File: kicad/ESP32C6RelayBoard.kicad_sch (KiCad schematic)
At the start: 118 parts, among them IC1 SPX1117M3-L-3-3_TR, J1 Screw_Terminal_01x02, J10 Screw_Terminal_01x03, J11 Screw_Terminal_01x03, J12 Screw_Terminal_01x03, J13 Screw_Terminal_01x03, J2 Conn_02x08_Odd_Even, J3 Screw_Terminal_01x02, J4 Screw_Terminal_01x02, J5 10118192-0001LF, J6 Screw_Terminal_01x02, J7 Screw_Terminal_01x02, J8 Screw_Terminal_01x03, J9 Screw_Terminal_01x03, K1 G5RL-K1-E-DC12, K2 G5RL-K1-E-DC12, K3 G5RL-K1-E-DC12, K4 G5RL-K1-E-DC12, Q1 FDN302P, U1 AP62300Z6-7, U10 INA232AIDDFR, U11 74HC237, U12 INA232AIDDFR, U13 FAN3241TMX, U14 FAN3241TMX, U2 ESP32-C6-MINI-1/U, U3 434133025816, U4 434133025816, U5 ESD401DPYR, U6 ESD401DPYR, U7 ESD401DPYR, U8 FAN3241TMX, U9 FAN3241TMX

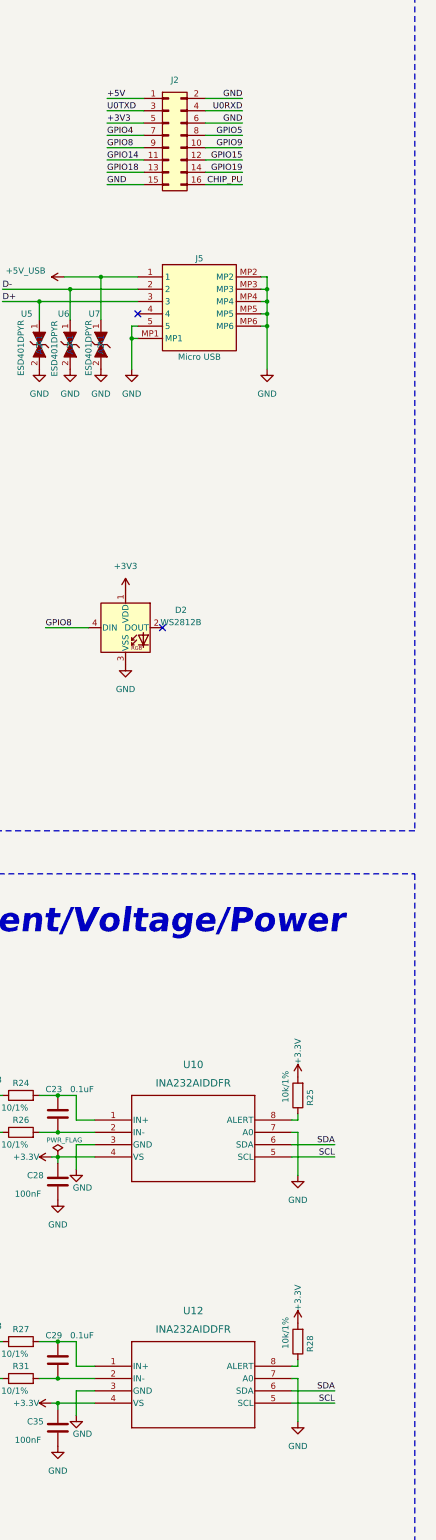
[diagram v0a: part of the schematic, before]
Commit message: Exposed also SCL and SDO on EXT connector
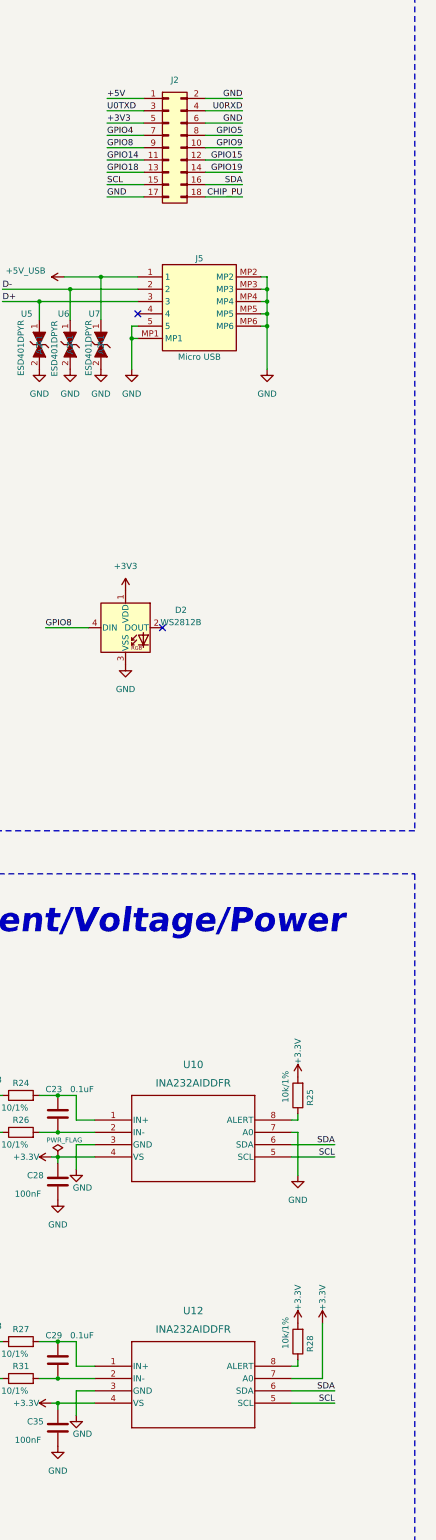
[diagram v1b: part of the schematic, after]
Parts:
- removed J2: Conn_02x08_Odd_Even, Connector_PinHeader_2.54mm:PinHeader_2x08_P2.54mm_Vertical, symbol Connector_Generic:Conn_02x08_Odd_Even
- added J2: Conn_02x09_Odd_Even, Connector_PinHeader_2.54mm:PinHeader_2x09_P2.54mm_Vertical, symbol Connector_Generic:Conn_02x09_Odd_Even
- U8: footprint (none) -> Onsemi:SOIC127P600X175-8N
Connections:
- net +3.3V: now also U12.7 (A0)
- net +3V3: now also J2.5 (Pin_5)
- net +5V: now also J2.1 (Pin_1)
- net CHIP_PU: now also J2.18 (Pin_18)
- net GND: now also J2.17 (Pin_17), J2.2 (Pin_2), J2.6 (Pin_6); no longer U12.7 (A0)
- net GPIO14: now also J2.11 (Pin_11)
- net GPIO15: now also J2.12 (Pin_12)
- net GPIO18: now also J2.13 (Pin_13)
- net GPIO19: now also J2.14 (Pin_14)
- net GPIO4: now also J2.7 (Pin_7)
- net GPIO5: now also J2.8 (Pin_8)
- net GPIO8: now also J2.9 (Pin_9)
- net GPIO9: now also J2.10 (Pin_10)
- net SCL: now also J2.15 (Pin_15)
- net SDA: now also J2.16 (Pin_16)
- net U0RXD: now also J2.4 (Pin_4)
- net U0TXD: now also J2.3 (Pin_3)
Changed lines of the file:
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@@
     (stroke (width 0) (type default))
   )
+  (wire (pts (xy 421.64 86.36) (xy 429.26 86.36))
+    (stroke (width 0) (type default))
+  )
   (wire (pts (xy 394.97 327.66) (xy 398.78 327.66))
     (stroke (width 0) (type default))
@@
     (stroke (width 0) (type default))
   )
-  (wire (pts (xy 421.64 83.82) (xy 429.26 83.82))
-    (stroke (width 0) (type default))
-  )
   (wire (pts (xy 128.27 152.4) (xy 128.27 154.94))
     (stroke (width 0) (type default))
@@
     (stroke (width 0) (type default))
   )
+  (wire (pts (xy 421.64 83.82) (xy 429.26 83.82))
+    (stroke (width 0) (type default))
+  )
   (wire (pts (xy 400.05 102.87) (xy 400.05 111.76))
     (stroke (width 0) (type default))
@@
     (stroke (width 0) (type default))
   )
-  (wire (pts (xy 439.42 330.2) (xy 440.69 330.2))
+  (wire (pts (xy 439.42 330.2) (xy 445.77 330.2))
     (stroke (width 0) (type default))
   )
@@
     (stroke (width 0) (type default))
   )
+  (wire (pts (xy 401.32 86.36) (xy 408.94 86.36))
+    (stroke (width 0) (type default))
+  )
   (wire (pts (xy 104.14 109.22) (xy 124.46 109.22))
     (stroke (width 0) (type default))
@@
     (stroke (width 0) (type default))
   )
-  (wire (pts (xy 440.69 330.2) (xy 440.69 339.09))
+  (wire (pts (xy 445.77 330.2) (xy 445.77 318.77))
     (stroke (width 0) (type default))
   )
@@
     (stroke (width 0) (type default))
   )
-  (wire (pts (xy 401.32 83.82) (xy 408.94 83.82))
-    (stroke (width 0) (type default))
-  )
   (wire (pts (xy 341.63 173.99) (xy 345.44 173.99))
     (stroke (width 0) (type default))
@@
     (stroke (width 0) (type default))
   )
+  (wire (pts (xy 401.32 83.82) (xy 408.94 83.82))
+    (stroke (width 0) (type default))
+  )
   (wire (pts (xy 110.49 85.09) (xy 129.54 85.09))
     (stroke (width 0) (type default))
@@
     (effects (font (size 1.27 1.27)) (justify right bottom))
   )
+  (label "GND" (at 401.32 86.36 0) (fields_autoplaced)
+    (effects (font (size 1.27 1.27)) (justify left bottom))
+  )
   (label "S{slash}R" (at 363.22 107.95 180) (fields_autoplaced)
     (effects (font (size 1.27 1.27)) (justify right bottom))
   )
+  (label "SDA" (at 429.26 83.82 180) (fields_autoplaced)
+    (effects (font (size 1.27 1.27)) (justify right bottom))
+  )
   (label "R0R" (at 77.47 306.07 180) (fields_autoplaced)
     (effects (font (size 1.27 1.27)) (justify right bottom))
@@
     (effects (font (size 1.27 1.27)) (justify left bottom))
   )
-  (label "GND" (at 401.32 83.82 0) (fields_autoplaced)
-    (effects (font (size 1.27 1.27)) (justify left bottom))
-  )
   (label "R3R" (at 219.71 344.17 0) (fields_autoplaced)
     (effects (font (size 1.27 1.27)) (justify left bottom))
@@
     (effects (font (size 1.27 1.27)) (justify left bottom))
   )
-  (label "CHIP_PU" (at 429.26 83.82 180) (fields_autoplaced)
-    (effects (font (size 1.27 1.27)) (justify right bottom))
-  )
   (label "GND" (at 429.26 71.12 180) (fields_autoplaced)
     (effects (font (size 1.27 1.27)) (justify right bottom))
@@
     (effects (font (size 1.27 1.27)) (justify right bottom))
   )
+  (label "SCL" (at 401.32 83.82 0) (fields_autoplaced)
+    (effects (font (size 1.27 1.27)) (justify left bottom))
+  )
   (label "D-" (at 379.73 105.41 0) (fields_autoplaced)
     (effects (font (size 1.27 1.27)) (justify left bottom))
@@
     (effects (font (size 1.27 1.27)) (justify right bottom))
   )
+  (label "CHIP_PU" (at 429.26 86.36 180) (fields_autoplaced)
+    (effects (font (size 1.27 1.27)) (justify right bottom))
+  )
   (label "ADC0" (at 283.21 72.39 0) (fields_autoplaced)
     (effects (font (size 1.27 1.27)) (justify left bottom))
@@
     )
   )
+  (symbol (lib_id "power:+3.3V") (at 445.77 318.77 0) (unit 1)
+    (in_bom yes) (on_board yes) (dnp no)
+    (property "Reference" "#PWR087" (at 445.77 322.58 0)
+      (effects (font (size 1.27 1.27)) hide)
+    )
+    (property "Value" "+3.3V" (at 445.77 316.23 90)
+      (effects (font (size 1.27 1.27)) (justify left))
+    )
+    (property "Footprint" "" (at 445.77 318.77 0)
+      (effects (font (size 1.27 1.27)) hide)
+    )
+    (property "Datasheet" "" (at 445.77 318.77 0)
+      (effects (font (size 1.27 1.27)) hide)
+    )
+    (pin "1")
+    (instances
+      (project "ESP32C6RelayBoard"
+        (path "/c75bdf3d-fde8-4fe0-9d0f-06bd3290cb63"
+          (reference "#PWR087") (unit 1)
+        )
+      )
+    )
+  )
   (symbol (lib_id "power:GND") (at 269.24 285.75 0) (unit 1)
     (in_bom yes) (on_board yes) (dnp no) (fields_autoplaced)
@@
     )
   )
+  (symbol (lib_id "Connector_Generic:Conn_02x09_Odd_Even") (at 414.02 76.2 0) (unit 1)
+    (in_bom yes) (on_board yes) (dnp no) (fields_autoplaced)
+    (property "Reference" "J2" (at 415.29 62.23 0)
+      (effects (font (size 1.27 1.27)))
+    )
+    (property "Value" "Conn_02x09_Odd_Even" (at 415.29 64.77 0)
+      (effects (font (size 1.27 1.27)) hide)
+    )
+    (property "Footprint" "Connector_PinHeader_2.54mm:PinHeader_2x09_P2.54mm_Vertical" (at 414.02 76.2 0)
+      (effects (font (size 1.27 1.27)) hide)
+    )
+    (property "Datasheet" "~" (at 414.02 76.2 0)
+      (effects (font (size 1.27 1.27)) hide)
+    )
+    (property "Number" "10129381-918001BLF" (at 414.02 76.2 0)
+      (effects (font (size 1.27 1.27)) hide)
+    )
+    (pin "16")
+    (pin "2")
+    (pin "3")
+    (pin "10")
+    (pin "15")
+    (pin "5")
+    (pin "7")
+    (pin "6")
+    (pin "11")
+    (pin "13")
+    (pin "9")
+    (pin "4")
+    (pin "1")
+    (pin "8")
+    (pin "14")
+    (pin "12")
+    (pin "18")
+    (pin "17")
+    (instances
+      (project "ESP32C6RelayBoard"
+        (path "/c75bdf3d-fde8-4fe0-9d0f-06bd3290cb63"
+          (reference "J2") (unit 1)
+        )
+      )
+    )
+  )
   (symbol (lib_id "Omron-G5RL:G5RL-K1-E-DC5_1") (at 311.15 294.64 270) (mirror x) (unit 1)
     (in_bom yes) (on_board yes) (dnp no)
@@
       (effects (font (size 1.27 1.27)))
     )
-    (property "Footprint" "" (at 123.19 273.05 0)
+    (property "Footprint" "Onsemi:SOIC127P600X175-8N" (at 123.19 273.05 0)
       (effects (font (size 1.27 1.27)) (justify bottom) hide)
     )
@@
     )
   )
-  (symbol (lib_id "power:GND") (at 440.69 339.09 0) (unit 1)
-    (in_bom yes) (on_board yes) (dnp no) (fields_autoplaced)
-    (property "Reference" "#PWR074" (at 440.69 345.44 0)
-      (effects (font (size 1.27 1.27)) hide)
-    )
-    (property "Value" "GND" (at 440.69 344.17 0)
-      (effects (font (size 1.27 1.27)))
-    )
-    (property "Footprint" "" (at 440.69 339.09 0)
-      (effects (font (size 1.27 1.27)) hide)
-    )
-    (property "Datasheet" "" (at 440.69 339.09 0)
-      (effects (font (size 1.27 1.27)) hide)
-    )
-    (pin "1")
-    (instances
-      (project "ESP32C6RelayBoard"
-        (path "/c75bdf3d-fde8-4fe0-9d0f-06bd3290cb63"
-          (reference "#PWR074") (unit 1)
-        )
-      )
-    )
-  )
   (symbol (lib_id "power:PWR_FLAG") (at 125.73 321.31 0) (unit 1)
     (in_bom yes) (on_board yes) (dnp no)
@@
         )
       )
-    )
-  )
-  (symbol (lib_id "Connector_Generic:Conn_02x08_Odd_Even") (at 414.02 73.66 0) (unit 1)
-    (in_bom yes) (on_board yes) (dnp no) (fields_autoplaced)
-    (property "Reference" "J2" (at 415.29 62.23 0)
-      (effects (font (size 1.27 1.27)))
-    )
-    (property "Value" "Conn_02x08_Odd_Even" (at 415.29 62.23 0)
-      (effects (font (size 1.27 1.27)) hide)
-    )
-    (property "Footprint" "Connector_PinHeader_2.54mm:PinHeader_2x08_P2.54mm_Vertical" (at 414.02 73.66 0)
-      (effects (font (size 1.27 1.27)) hide)
-    )
-    (property "Datasheet" "~" (at 414.02 73.66 0)
-      (effects (font (size 1.27 1.27)) hide)
-    )
-    (property "Number" "10129381-908002BLF" (at 414.02 73.66 0)
-      (effects (font (size 1.27 1.27)) hide)
-    )
-    (pin "16")
-    (pin "2")
-    (pin "3")
-    (pin "10")
-    (pin "15")
-    (pin "5")
-    (pin "7")
-    (pin "6")
-    (pin "11")
-    (pin "13")
-    (pin "9")
-    (pin "4")
-    (pin "1")
-    (pin "8")
-    (pin "14")
-    (pin "12")
-    (instances
-      (project "ESP32C6RelayBoard"
-        (path "/c75bdf3d-fde8-4fe0-9d0f-06bd3290cb63"
-          (reference "J2") (unit 1)
-        )
-      )

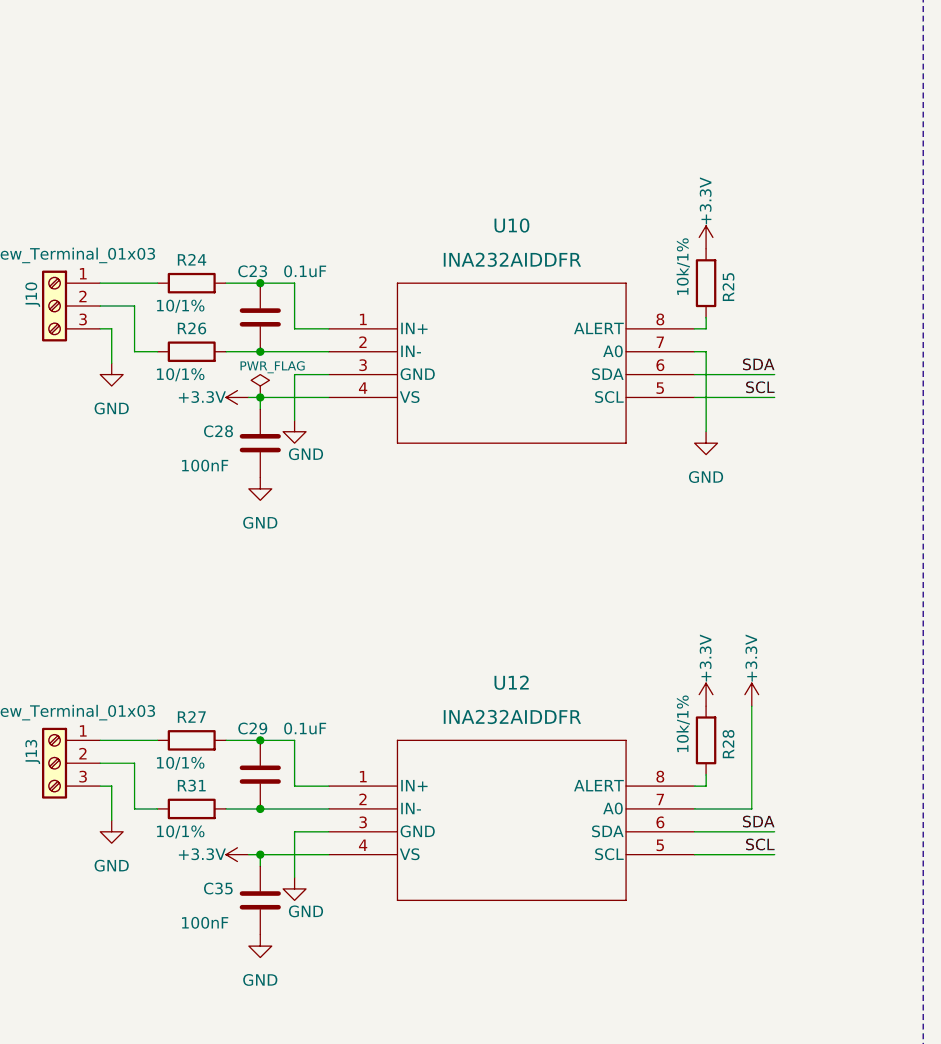
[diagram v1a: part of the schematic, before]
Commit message: Added 3D models to the project
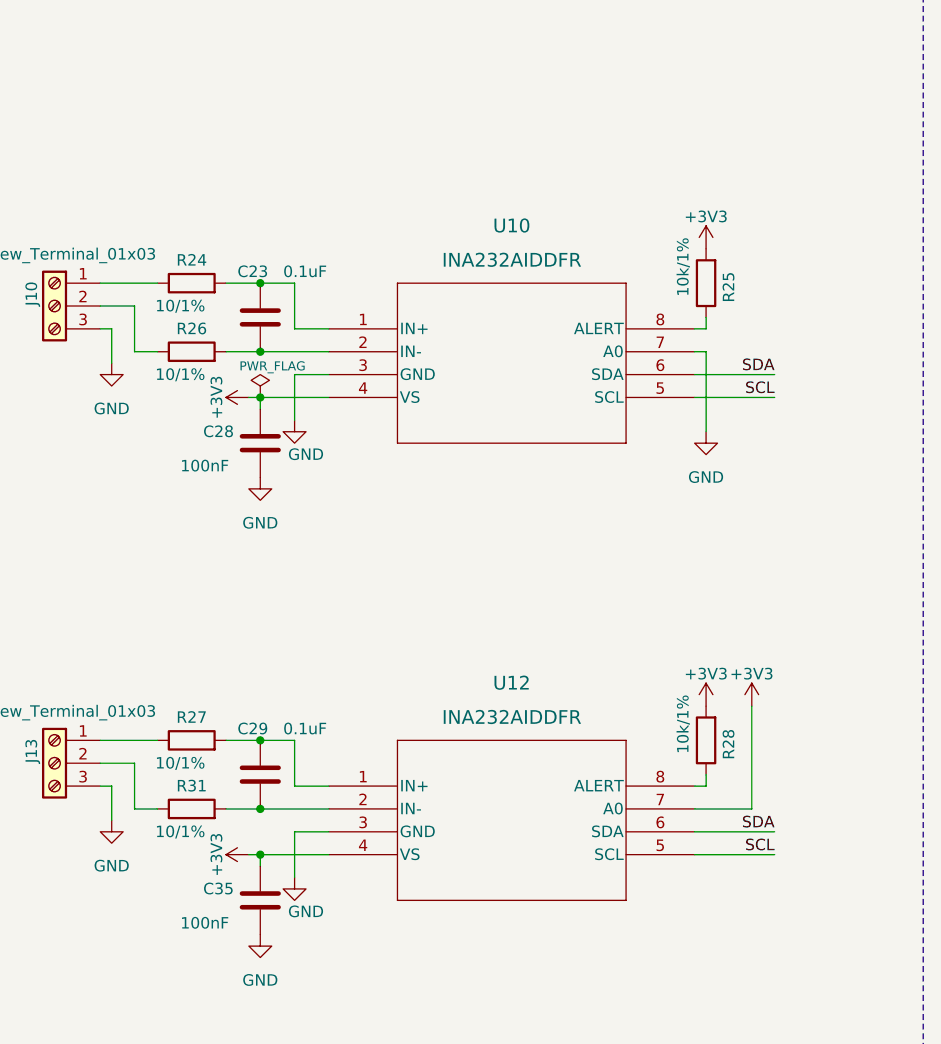
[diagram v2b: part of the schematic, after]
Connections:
- net +3.3V is gone; now on net +3V3: C28.1, C35.1, R25.2, R28.2, U10.4 (VS), U12.4 (VS), U12.7 (A0)
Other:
- title: ESP32C6 Mini relay board -> ESP32C6 Mini - Latching relay board
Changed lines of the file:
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@@
   (paper "A2")
   (title_block
-    (title "ESP32C6 Mini relay board")
+    (title "ESP32C6 Mini - Latching relay board")
     (date "2023-11-15")
   )
@@
     )
   )
-  (symbol (lib_id "power:+3.3V") (at 389.89 284.48 90) (unit 1)
+  (symbol (lib_id "power:+3V3") (at 389.89 284.48 90) (unit 1)
     (in_bom yes) (on_board yes) (dnp no)
     (property "Reference" "#PWR053" (at 393.7 284.48 0)
       (effects (font (size 1.27 1.27)) hide)
     )
-    (property "Value" "+3.3V" (at 387.35 284.48 90)
-      (effects (font (size 1.27 1.27)) (justify left))
+    (property "Value" "+3V3" (at 386.334 284.48 0)
+      (effects (font (size 1.27 1.27)))
     )
     (property "Footprint" "" (at 389.89 284.48 0)
@@
     )
   )
-  (symbol (lib_id "power:+3.3V") (at 445.77 318.77 0) (unit 1)
+  (symbol (lib_id "power:+3V3") (at 445.77 318.77 0) (unit 1)
     (in_bom yes) (on_board yes) (dnp no)
     (property "Reference" "#PWR087" (at 445.77 322.58 0)
       (effects (font (size 1.27 1.27)) hide)
     )
-    (property "Value" "+3.3V" (at 445.77 316.23 90)
-      (effects (font (size 1.27 1.27)) (justify left))
+    (property "Value" "+3V3" (at 445.77 315.214 0)
+      (effects (font (size 1.27 1.27)))
     )
     (property "Footprint" "" (at 445.77 318.77 0)
@@
     )
   )
-  (symbol (lib_id "power:+3.3V") (at 389.89 335.28 90) (unit 1)
+  (symbol (lib_id "power:+3V3") (at 389.89 335.28 90) (unit 1)
     (in_bom yes) (on_board yes) (dnp no)
     (property "Reference" "#PWR072" (at 393.7 335.28 0)
       (effects (font (size 1.27 1.27)) hide)
     )
-    (property "Value" "+3.3V" (at 387.35 335.28 90)
-      (effects (font (size 1.27 1.27)) (justify left))
+    (property "Value" "+3V3" (at 386.334 335.28 0)
+      (effects (font (size 1.27 1.27)))
     )
     (property "Footprint" "" (at 389.89 335.28 0)
@@
     )
   )
-  (symbol (lib_id "power:+3.3V") (at 440.69 318.77 0) (unit 1)
+  (symbol (lib_id "power:+3V3") (at 440.69 318.77 0) (unit 1)
     (in_bom yes) (on_board yes) (dnp no)
     (property "Reference" "#PWR068" (at 440.69 322.58 0)
       (effects (font (size 1.27 1.27)) hide)
     )
-    (property "Value" "+3.3V" (at 440.69 316.23 90)
-      (effects (font (size 1.27 1.27)) (justify left))
+    (property "Value" "+3V3" (at 440.69 315.214 0)
+      (effects (font (size 1.27 1.27)))
     )
     (property "Footprint" "" (at 440.69 318.77 0)
@@
     )
   )
-  (symbol (lib_id "power:+3.3V") (at 440.69 267.97 0) (unit 1)
+  (symbol (lib_id "power:+3V3") (at 440.69 267.97 0) (unit 1)
     (in_bom yes) (on_board yes) (dnp no)
     (property "Reference" "#PWR051" (at 440.69 271.78 0)
       (effects (font (size 1.27 1.27)) hide)
     )
-    (property "Value" "+3.3V" (at 440.69 265.43 90)
-      (effects (font (size 1.27 1.27)) (justify left))
+    (property "Value" "+3V3" (at 440.69 264.414 0)
+      (effects (font (size 1.27 1.27)))
     )
     (property "Footprint" "" (at 440.69 267.97 0)
